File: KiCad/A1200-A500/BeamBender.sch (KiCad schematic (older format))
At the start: 71 parts, among them J1 4-1734742-0, J2 HDMI_A_1.4, J3 STX-3501-3N, J4 Phoenix_Contact, J5 Conn_01x01, U1 LM1117-3.3, U3 ADV7513BSWZ, U4 MCP1702T-1802E_CB, X1 Abracon ASE-27.000MHZ-L-R-T, X2 Oscillator_7.0x5.0mm

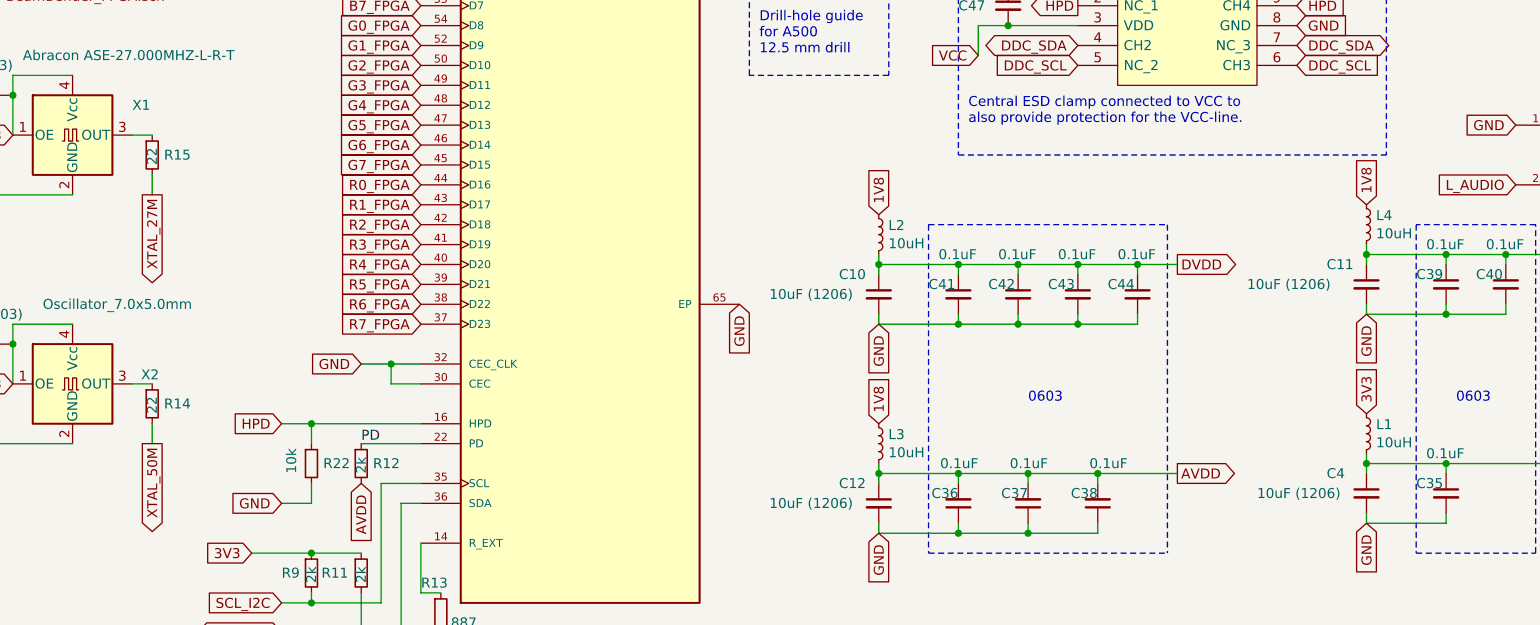
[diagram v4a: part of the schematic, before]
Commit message: Fixed ordering of L1-L4, changed R14-R21 to 33 Ohms, and swapped X2 and X3 reference
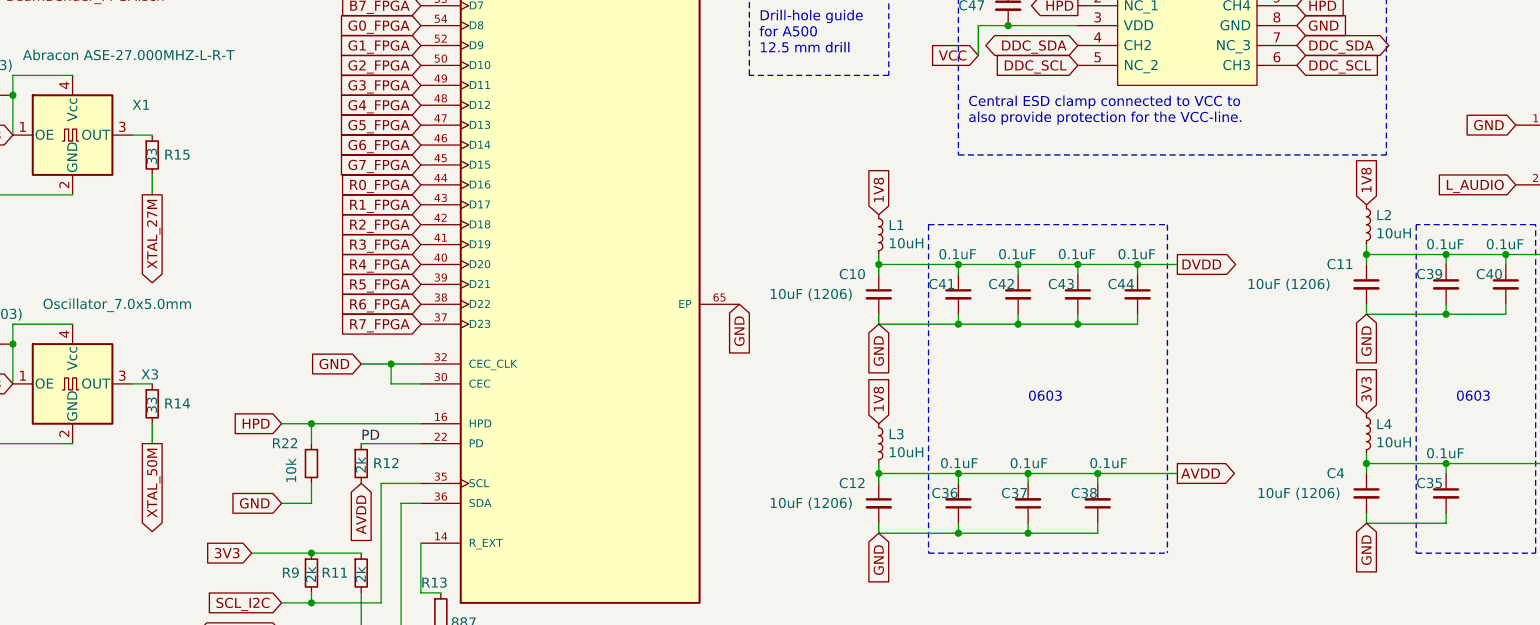
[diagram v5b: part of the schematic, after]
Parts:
- R14, R15: value 22 -> 33
- renumbered L2 to L1, L4 to L2, L1 to L4, X2 to X3
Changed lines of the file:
@@
 P 3050 4350
 F 0 "R15" H 3109 4350 50  0000 L CNN
-F 1 "22" V 3050 4300 50  0000 L CNN
+F 1 "33" V 3050 4300 50  0000 L CNN
 F 2 "Resistor_SMD:R_0603_1608Metric_Pad0.98x0.95mm_HandSolder" H 3050 4350 50  0001 C CNN
 F 3 "~" H 3050 4350 50  0001 C CNN
@@
 	6700 5150 6700 5200
 $Comp
-L Oscillator:SG-8002CA X2
+L Oscillator:SG-8002CA X3
 U 1 1 658825BB
 P 2650 5500
-F 0 "X2" H 2994 5546 50  0000 L CNN
+F 0 "X3" H 2994 5546 50  0000 L CNN
 F 1 "Oscillator_7.0x5.0mm" H 2500 5900 50  0000 L CNN
 F 2 "Oscillator:Oscillator_SMD_SeikoEpson_SG8002CA-4Pin_7.0x5.0mm_HandSoldering" H 3350 5150 50  0001 C CNN
@@
 P 3050 5600
 F 0 "R14" H 3109 5600 50  0000 L CNN
-F 1 "22" V 3050 5550 50  0000 L CNN
+F 1 "33" V 3050 5550 50  0000 L CNN
 F 2 "Resistor_SMD:R_0603_1608Metric_Pad0.98x0.95mm_HandSolder" H 3050 5600 50  0001 C CNN
 F 3 "~" H 3050 5600 50  0001 C CNN
@@
 1V8
 $Comp
-L Device:L_Small L2
+L Device:L_Small L1
 U 1 1 65D34DF4
 P 6700 4750
-F 0 "L2" H 6748 4796 50  0000 L CNN
+F 0 "L1" H 6748 4796 50  0000 L CNN
 F 1 "10uH" H 6748 4705 50  0000 L CNN
 F 2 "Capacitor_SMD:C_0805_2012Metric_Pad1.18x1.45mm_HandSolder" H 6700 4750 50  0001 C CNN
@@
 1V8
 $Comp
-L Device:L_Small L4
+L Device:L_Small L2
 U 1 1 65ED6CCA
 P 9150 4700
-F 0 "L4" H 9198 4746 50  0000 L CNN
+F 0 "L2" H 9198 4746 50  0000 L CNN
 F 1 "10uH" H 9198 4655 50  0000 L CNN
 F 2 "Capacitor_SMD:C_0805_2012Metric_Pad1.18x1.45mm_HandSolder" H 9150 4700 50  0001 C CNN
@@
 3V3
 $Comp
-L Device:L_Small L1
+L Device:L_Small L4
 U 1 1 65CC8700
 P 9150 5750
-F 0 "L1" H 9198 5796 50  0000 L CNN
+F 0 "L4" H 9198 5796 50  0000 L CNN
 F 1 "10uH" H 9198 5705 50  0000 L CNN
 F 2 "Capacitor_SMD:C_0805_2012Metric_Pad1.18x1.45mm_HandSolder" H 9150 5750 50  0001 C CNN
@@
 U 1 1 652DC9C5
 P 3850 5900
-F 0 "R22" H 3909 5900 50  0000 L CNN
-F 1 "10k" V 3750 5850 50  0000 L CNN
+F 0 "R22" H 3650 6000 50  0000 L CNN
+F 1 "10k" V 3750 5800 50  0000 L CNN
 F 2 "Resistor_SMD:R_0603_1608Metric_Pad0.98x0.95mm_HandSolder" H 3850 5900 50  0001 C CNN
 F 3 "~" H 3850 5900 50  0001 C CNN

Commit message: Changed R12 to a selectable pull-up/pull-down three-pads footprint
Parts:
- R12: footprint Resistor_SMD:R_0603_1608Metric_Pad0.98x0.95mm_HandSolder -> BeamBender:ResistorJumper-3_Open_Pad_0603; symbol Device:R_Small -> BeamBender:Resistor_Jumper_Small
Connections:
- net AVDD: now also R12.3; no longer R12.2
- net GND: now also R12.1
- net PD: now also R12.2; no longer R12.1
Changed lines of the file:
@@
 	4100 5800 4400 5800
 $Comp
-L Device:R_Small R12
+L BeamBender:Resistor_Jumper_Small R12
 U 1 1 6531102F
 P 4100 5900
-F 0 "R12" H 4159 5900 50  0000 L CNN
+F 0 "R12" V 4200 5800 50  0000 L CNN
 F 1 "2k" V 4100 5850 50  0000 L CNN
-F 2 "Resistor_SMD:R_0603_1608Metric_Pad0.98x0.95mm_HandSolder" H 4100 5900 50  0001 C CNN
+F 2 "BeamBender:ResistorJumper-3_Open_Pad_0603" H 4100 5900 50  0001 C CNN
 F 3 "~" H 4100 5900 50  0001 C CNN
 	1    4100 5900
-	1    0    0    -1
+	0    1    1    0
 $EndComp
 Wire Wire Line
@@
 	8000 5200 8000 5150
 Connection ~ 7700 5200
-Text GLabel 4100 6000 3    50   Input ~ 0
+Text GLabel 3950 6050 3    50   Input ~ 0
 AVDD
 $Comp
@@
 	1    0    0    -1
 $EndComp
+Wire Wire Line
+	4100 5800 4100 5850
+Wire Wire Line
+	4000 5900 3950 5900
+Wire Wire Line
+	3950 5900 3950 6050
+Text GLabel 4250 5900 2    50   Input ~ 0
+GND
+Wire Wire Line
+	4200 5900 4250 5900
 $EndSCHEMATC

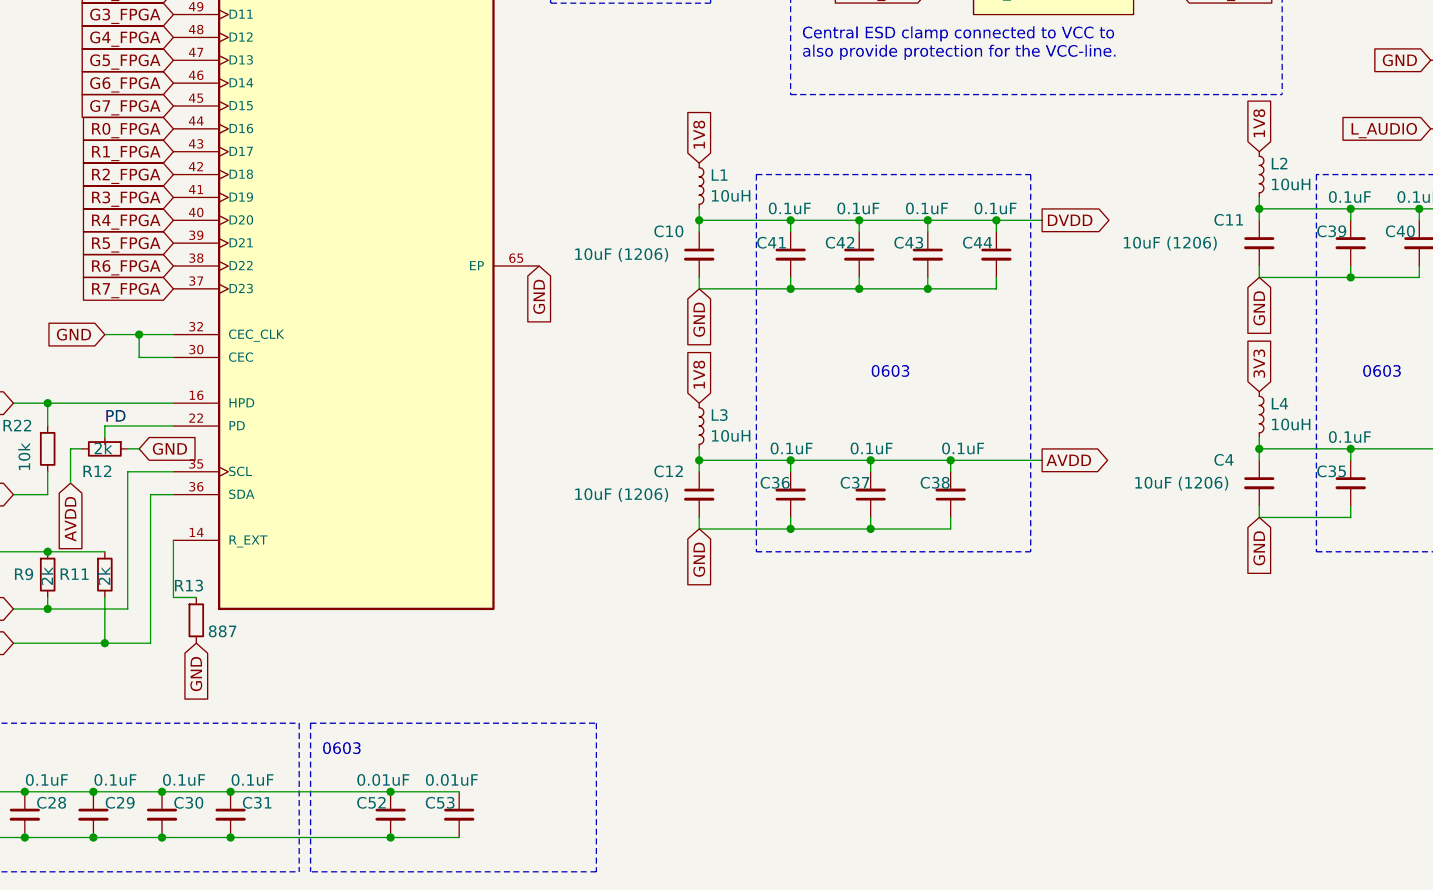
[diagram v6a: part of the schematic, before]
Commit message: Adapted design to take 1.8V on VCCIO3 because of embedded pSRAM requirement, changed RN1, RN2 to 4.7k Ohm, relocated pin FSEL and DIF/TDMI to bank0, moved PDN_RESET_N to pin 29 and MCLK to pin 30. JP2 to pin 28, pin 7,8,12,23 changed to NC from GND, added pull-up for JTAG_TDO signal.
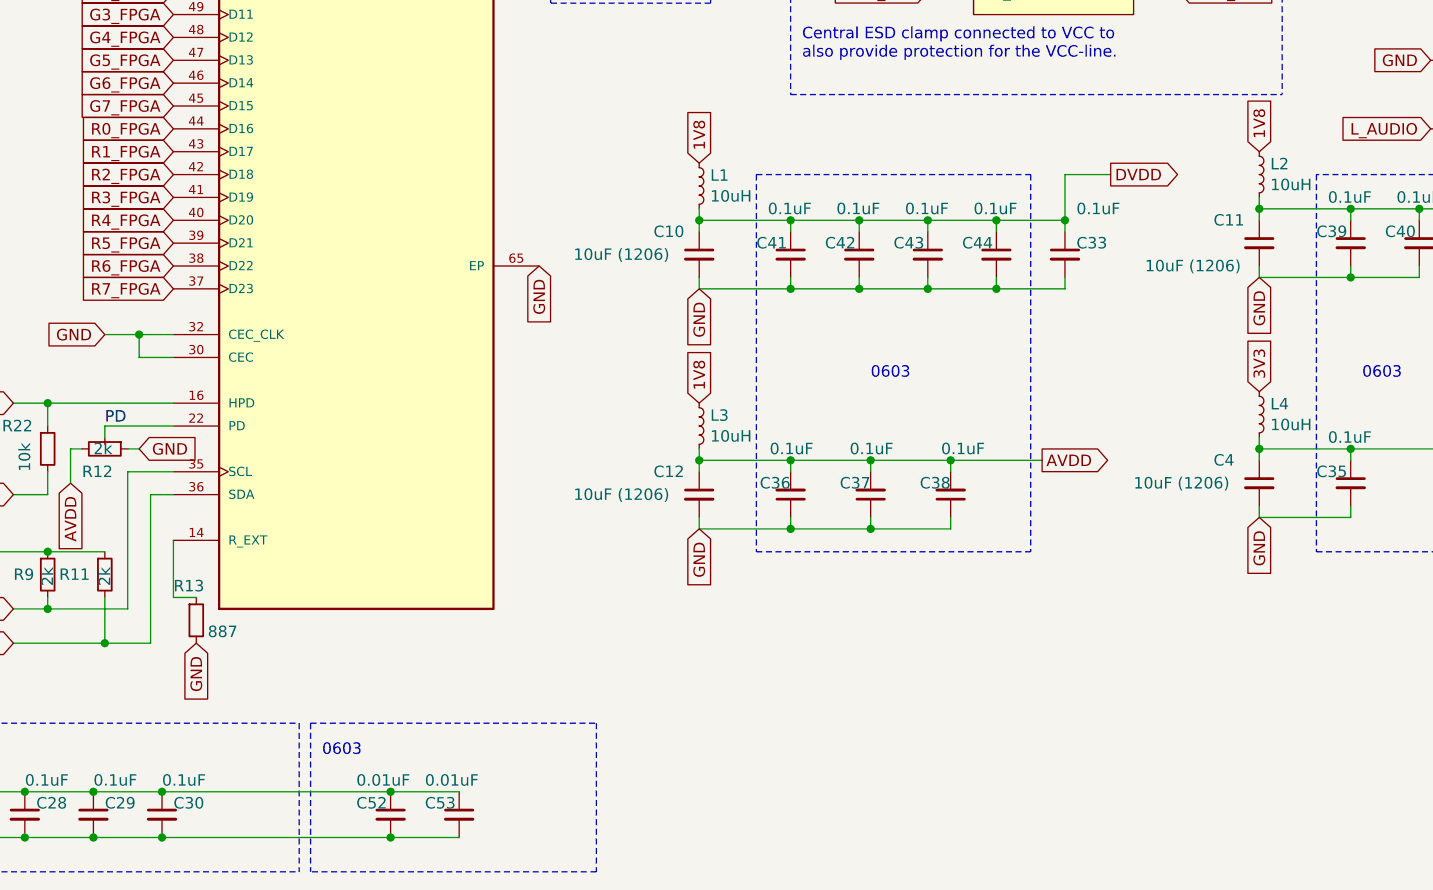
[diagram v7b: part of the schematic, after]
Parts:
- renumbered C30 to C29, C31 to C30, C29 to C33
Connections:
- net 3V3: no longer C33.2
- net DVDD: now also C33.1
- net GND: now also C33.2; no longer C33.1
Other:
- moved on the sheet: C29, C30, C33
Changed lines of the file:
@@
 DVDD_3V
 $Comp
-L Device:C_Small C30
+L Device:C_Small C29
 U 1 1 6563C1E1
-P 4350 7500
-F 0 "C30" H 4400 7550 50  0000 L CNN
-F 1 "0.1uF" H 4350 7650 50  0000 L CNN
-F 2 "Capacitor_SMD:C_0805_2012Metric_Pad1.18x1.45mm_HandSolder" H 4350 7500 50  0001 C CNN
-F 3 "~" H 4350 7500 50  0001 C CNN
-	1    4350 7500
+P 4050 7500
+F 0 "C29" H 4100 7550 50  0000 L CNN
+F 1 "0.1uF" H 4050 7650 50  0000 L CNN
+F 2 "Capacitor_SMD:C_0805_2012Metric_Pad1.18x1.45mm_HandSolder" H 4050 7500 50  0001 C CNN
+F 3 "~" H 4050 7500 50  0001 C CNN
+	1    4050 7500
 	1    0    0    -1
 $EndComp
@@
 	1    0    0    -1
 $EndComp
-Text GLabel 8200 4900 2    50   Output ~ 0
+Text GLabel 8500 4700 2    50   Output ~ 0
 DVDD
 $Comp
@@
 	2100 5300 2150 5300
 $Comp
-L Device:C_Small C31
+L Device:C_Small C30
 U 1 1 6591CDE3
-P 4650 7500
-F 0 "C31" H 4700 7550 50  0000 L CNN
-F 1 "0.1uF" H 4650 7650 50  0000 L CNN
-F 2 "Capacitor_SMD:C_0805_2012Metric_Pad1.18x1.45mm_HandSolder" H 4650 7500 50  0001 C CNN
-F 3 "~" H 4650 7500 50  0001 C CNN
-	1    4650 7500
+P 4350 7500
+F 0 "C30" H 4400 7550 50  0000 L CNN
+F 1 "0.1uF" H 4350 7650 50  0000 L CNN
+F 2 "Capacitor_SMD:C_0805_2012Metric_Pad1.18x1.45mm_HandSolder" H 4350 7500 50  0001 C CNN
+F 3 "~" H 4350 7500 50  0001 C CNN
+	1    4350 7500
 	1    0    0    -1
 $EndComp
@@
 P 9150 5000
 F 0 "C11" H 8950 5100 50  0000 L CNN
-F 1 "10uF (1206)" H 8550 5000 50  0000 L CNN
+F 1 "10uF (1206)" H 8650 4900 50  0000 L CNN
 F 2 "Capacitor_SMD:C_1206_3216Metric_Pad1.33x1.80mm_HandSolder" H 9150 5000 50  0001 C CNN
 F 3 "~" H 9150 5000 50  0001 C CNN
@@
 Text Notes 6100 3850 0    50   ~ 0
 Drill-hole guide\nfor A500 \n12.5 mm drill
-Wire Wire Line
-	3750 7400 4050 7400
-Wire Wire Line
-	3750 7600 4050 7600
-$Comp
-L Device:C_Small C29
+$Comp
+L Device:C_Small C33
 U 1 1 6639D585
-P 4050 7500
-F 0 "C29" H 4100 7550 50  0000 L CNN
-F 1 "0.1uF" H 4050 7650 50  0000 L CNN
-F 2 "Capacitor_SMD:C_0805_2012Metric_Pad1.18x1.45mm_HandSolder" H 4050 7500 50  0001 C CNN
-F 3 "~" H 4050 7500 50  0001 C CNN
-	1    4050 7500
-	1    0    0    -1
-$EndComp
-Connection ~ 4050 7400
-Wire Wire Line
-	4050 7400 4350 7400
-Connection ~ 4050 7600
-Wire Wire Line
-	4050 7600 4350 7600
+P 8300 5050
+F 0 "C33" H 8350 5100 50  0000 L CNN
+F 1 "0.1uF" H 8350 5250 50  0000 L CNN
+F 2 "Capacitor_SMD:C_0805_2012Metric_Pad1.18x1.45mm_HandSolder" H 8300 5050 50  0001 C CNN
+F 3 "~" H 8300 5050 50  0001 C CNN
+	1    8300 5050
+	1    0    0    -1
+$EndComp
 $Comp
 L Device:C_Small C28
@@
 	1    0    0    -1
 $EndComp
-Connection ~ 4350 7400
 Connection ~ 4350 7600
 $Comp
@@
 	1    0    0    -1
 $EndComp
-Wire Wire Line
-	4350 7400 4650 7400
-Wire Wire Line
-	4350 7600 4650 7600
 Wire Notes Line
 	5000 7100 5000 7750
 Wire Wire Line
-	4650 7400 5350 7400
-Connection ~ 4650 7400
-Connection ~ 5350 7400
-Wire Wire Line
 	5350 7400 5650 7400
-Wire Wire Line
-	4650 7600 5350 7600
-Connection ~ 4650 7600
 Connection ~ 5350 7600
 Wire Wire Line
@@
 0603
 Wire Wire Line
-	8000 4900 8200 4900
-Wire Wire Line
 	7800 5950 8200 5950
 Wire Notes Line
@@
 Wire Wire Line
 	4200 5900 4250 5900
+Wire Wire Line
+	8300 4950 8300 4900
+Wire Wire Line
+	3750 7400 4050 7400
+Wire Wire Line
+	3750 7600 4050 7600
+Wire Wire Line
+	8000 4900 8300 4900
+Wire Wire Line
+	8300 4900 8300 4700
+Wire Wire Line
+	8300 4700 8500 4700
+Connection ~ 8300 4900
+Wire Wire Line
+	8000 5200 8300 5200
+Wire Wire Line
+	8300 5200 8300 5150
+Connection ~ 8000 5200
+Connection ~ 4050 7400
+Wire Wire Line
+	4050 7400 4350 7400
+Connection ~ 4050 7600
+Wire Wire Line
+	4050 7600 4350 7600
+Connection ~ 5350 7400
+Connection ~ 4350 7400
+Wire Wire Line
+	4350 7400 5350 7400
+Wire Wire Line
+	4350 7600 5350 7600
 $EndSCHEMATC

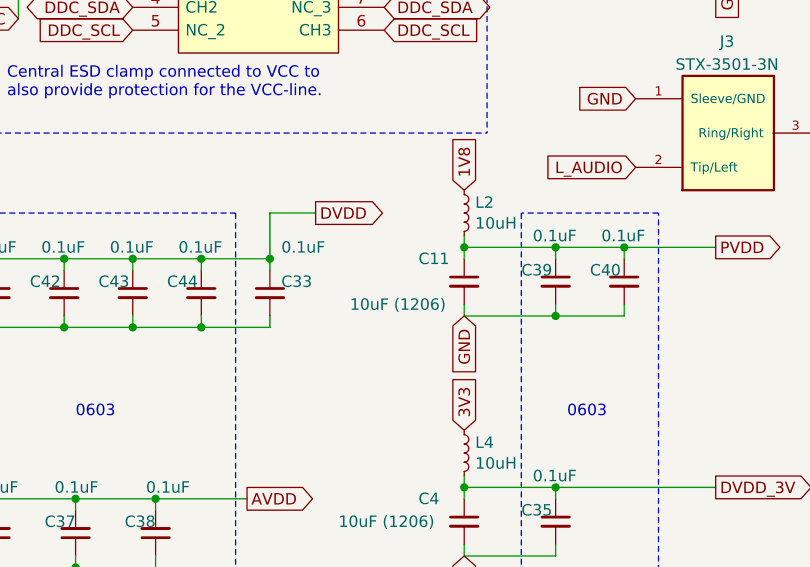
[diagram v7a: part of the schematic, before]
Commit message: Added decoupling cap C55 (10nF 0603) to VCCIO3-input (DVDD)
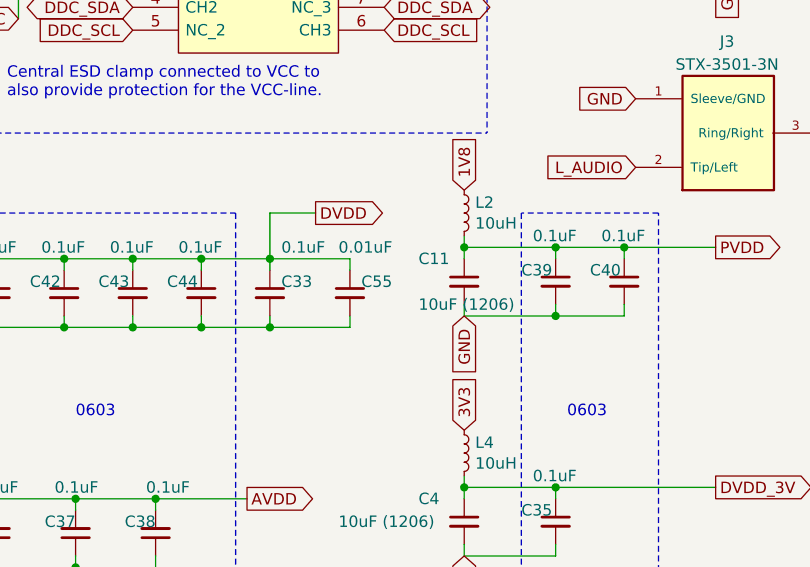
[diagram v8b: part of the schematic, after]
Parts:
- added C55: 0.01uF, Capacitor_SMD:C_0603_1608Metric_Pad1.08x0.95mm_HandSolder, symbol Device:C_Small
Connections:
- net DVDD: now also C55.1
- net GND: now also C55.2
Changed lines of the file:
@@
 P 9150 5000
 F 0 "C11" H 8950 5100 50  0000 L CNN
-F 1 "10uF (1206)" H 8650 4900 50  0000 L CNN
+F 1 "10uF (1206)" H 8950 4900 50  0000 L CNN
 F 2 "Capacitor_SMD:C_1206_3216Metric_Pad1.33x1.80mm_HandSolder" H 9150 5000 50  0001 C CNN
 F 3 "~" H 9150 5000 50  0001 C CNN
@@
 Wire Wire Line
 	4350 7600 5350 7600
+$Comp
+L Device:C_Small C55
+U 1 1 66DA5578
+P 8650 5050
+F 0 "C55" H 8700 5100 50  0000 L CNN
+F 1 "0.01uF" H 8600 5250 50  0000 L CNN
+F 2 "Capacitor_SMD:C_0603_1608Metric_Pad1.08x0.95mm_HandSolder" H 8650 5050 50  0001 C CNN
+F 3 "~" H 8650 5050 50  0001 C CNN
+	1    8650 5050
+	1    0    0    -1
+$EndComp
+Wire Wire Line
+	8300 4900 8650 4900
+Wire Wire Line
+	8650 4900 8650 4950
+Wire Wire Line
+	8300 5200 8650 5200
+Wire Wire Line
+	8650 5200 8650 5150
+Connection ~ 8300 5200
 $EndSCHEMATC
